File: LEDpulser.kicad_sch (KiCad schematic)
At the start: 70 parts, among them J1 RJHSE-5380, J2 EPS.00.250.NTN, J3 EPS.00.250.NTN, J4 EB21A-04-D, J5 EPL.0S.302.HLN, Q1 BVSS84LT1G, Q2 DMN3028LQ-7, Q3 DMN3028LQ-7, SW1 BST11T2AVR, U1 74AHCT123APW,118, U10 LT3082EST#TRPBF, U2 74AHCT123APW,118, U3 74AHCT123APW,118, U4 SN74LVC2G74, U5 LT1117, U6 IXDI602SIATR, U7 NE555S-13, U8 PM8834, U9 PM8834

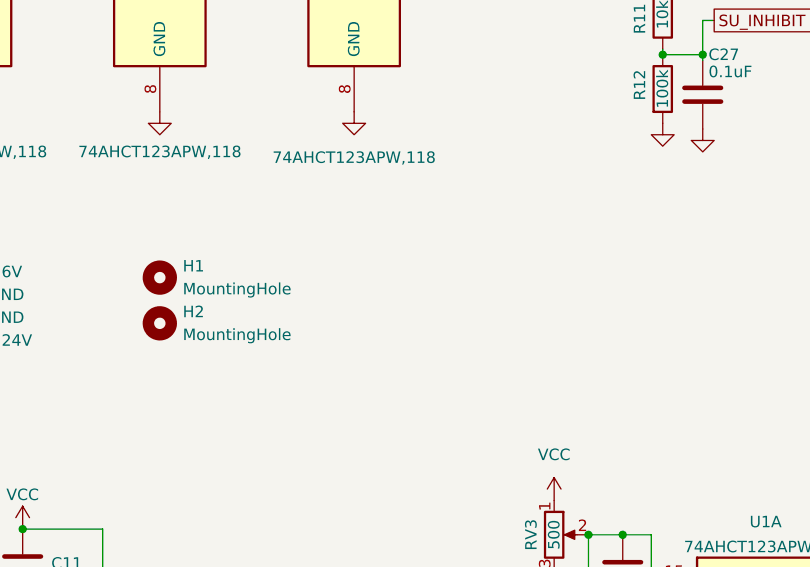
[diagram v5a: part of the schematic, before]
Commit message: Added third mounting hole. Added cutout for LEMO-connector back-side nuts.
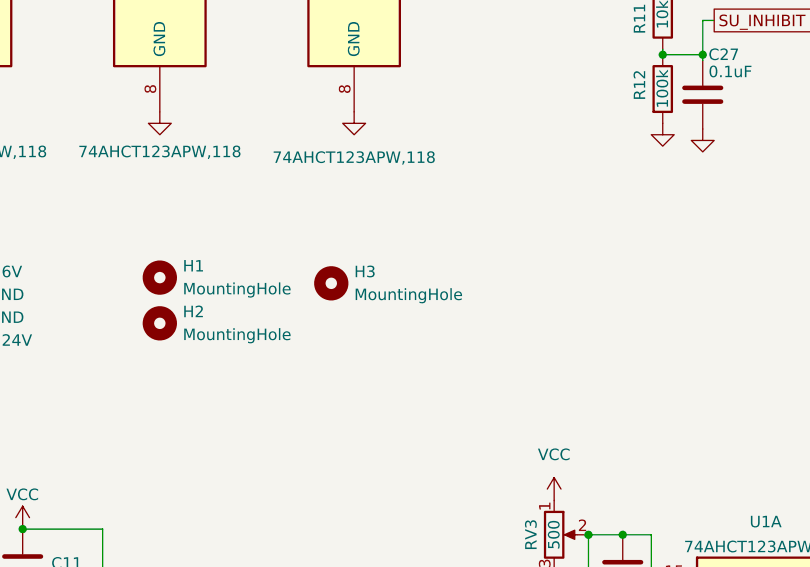
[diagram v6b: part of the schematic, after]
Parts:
- added H3: MountingHole, MountingHole:MountingHole_3.2mm_M3, symbol Mechanical:MountingHole
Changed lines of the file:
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@@
   (symbol (lib_id "power:VCC") (at 55.245 208.28 180) (unit 1)
     (in_bom yes) (on_board yes)
-    (property "Reference" "#PWR?" (id 0) (at 55.245 204.47 0)
+    (property "Reference" "#PWR0120" (id 0) (at 55.245 204.47 0)
       (effects (font (size 1.27 1.27)) hide)
     )
@@
     (pin "1")
   )
+  (symbol (lib_id "Mechanical:MountingHole") (at 72.39 64.77 0) (unit 1)
+    (in_bom yes) (on_board yes) (fields_autoplaced)
+    (property "Reference" "H3" (id 0) (at 74.93 63.4999 0)
+      (effects (font (size 1.27 1.27)) (justify left))
+    )
+    (property "Value" "MountingHole" (id 1) (at 74.93 66.0399 0)
+      (effects (font (size 1.27 1.27)) (justify left))
+    )
+    (property "Footprint" "MountingHole:MountingHole_3.2mm_M3" (id 2) (at 72.39 64.77 0)
+      (effects (font (size 1.27 1.27)) hide)
+    )
+    (property "Datasheet" "~" (id 3) (at 72.39 64.77 0)
+      (effects (font (size 1.27 1.27)) hide)
+    )
+  )
   (symbol (lib_id "power:VCC") (at 38.1 92.075 0) (unit 1)
     (in_bom yes) (on_board yes)
@@
       (reference "#PWR0119") (unit 1) (value "GND") (footprint "")
     )
+    (path "/3407777c-d948-490d-a2f0-b3ad3390e217"
+      (reference "#PWR0120") (unit 1) (value "VCC") (footprint "")
+    )
     (path "/b48ba73f-35c5-4fb7-bedf-312e98c2ff95"
       (reference "#PWR0121") (unit 1) (value "GND") (footprint "")
@@
       (reference "#PWR0177") (unit 1) (value "GND") (footprint "")
     )
-    (path "/3407777c-d948-490d-a2f0-b3ad3390e217"
-      (reference "#PWR?") (unit 1) (value "VCC") (footprint "")
-    )
     (path "/f93b1b9a-0026-469f-bb79-98b3a8c675dd"
       (reference "C1") (unit 1) (value "0.1uF") (footprint "Capacitor_SMD:C_0603_1608Metric")
@@
       (reference "H2") (unit 1) (value "MountingHole") (footprint "MountingHole:MountingHole_3.2mm_M3")
     )
+    (path "/7d646651-5aef-453f-ad93-710225b27da3"
+      (reference "H3") (unit 1) (value "MountingHole") (footprint "MountingHole:MountingHole_3.2mm_M3")
+    )
     (path "/9488ae24-3cd4-4e78-897c-a03dbef50cd8"

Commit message: Added series resistors for pots.
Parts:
- added R13: 22, Resistor_SMD:R_0603_1608Metric, symbol Device:R
- added R14, R15, R16, R17, R18, R19, R20, R21, R22, R23, R24: 0, Resistor_SMD:R_0603_1608Metric, symbol Device:R
- added R25: DNP, Resistor_SMD:R_0603_1608Metric, symbol Device:R
- Q1: value BVSS84LT1G -> DMP32D4S; VGS(th) VGS(th) -0.9V to -2.0V -> VGS(th) -1.4V to -2.4V
- R2: value 1k -> 10k
- RV1: value 2k -> 2Meg; Part# Y50532K00000J0L -> 3296Z-1-205LF; TemperatureCoefficient 10ppm/C -> 100ppm/C
- RV2, RV3: value 500 -> 2k
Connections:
- net CAP_CHARGING_OUT: now also R23.2; no longer Q1.1 (G)
- net CAP_VOLTAGE_OUT: now also R24.2; no longer Q1.2 (S)
- net LED_ON_OUT: now also R22.2; no longer Q2.1 (G)
- net LED_SHORT_OUT: now also R21.2; no longer Q3.1 (G)
- net VCC: now also R25.1
- net at C7.1, U10.1 (ADJ): now also R20.2; no longer RV1.2, RV1.3
- net at RV4.2, RV4.3: now also R18.1; no longer C14.1, U2.7 (RCext)
- net at RV3.2, RV3.3: now also R15.1; no longer C13.1, U1.15 (RCext)
- net at RV6.2, RV6.3: now also R17.1; no longer C19.1, U3.15 (RCext)
- net at C20.1, U3.7 (RCext): now also R19.2; no longer RV7.2, RV7.3
- net at C18.1, U7.2 (TR), U7.6 (THR): now also R13.2, R25.2; no longer RV5.2, RV5.3
- net at C8.2, U2.15 (RCext): now also R16.2; no longer RV2.2, RV2.3
- net at RV8.2, RV8.3: now also R14.2; no longer C25.1, U1.7 (RCext)
- new net: R13.1, RV5.2, RV5.3
- new net: Q1.2 (S), R24.1
- new net: C14.1, R18.2, U2.7 (RCext)
- new net: C13.1, R15.2, U1.15 (RCext)
- new net: R16.1, RV2.2, RV2.3
- new net: R19.1, RV7.2, RV7.3
- new net: C19.1, R17.2, U3.15 (RCext)
- new net: C25.1, R14.1, U1.7 (RCext)
- new net: Q1.1 (G), R23.1
- new net: Q2.1 (G), R22.1
- new net: Q3.1 (G), R21.1
- new net: R20.1, RV1.2, RV1.3
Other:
- moved on the sheet: C19, C24, C26, C5, C7, D2, J1, RV1, RV2, RV3, RV4, RV5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

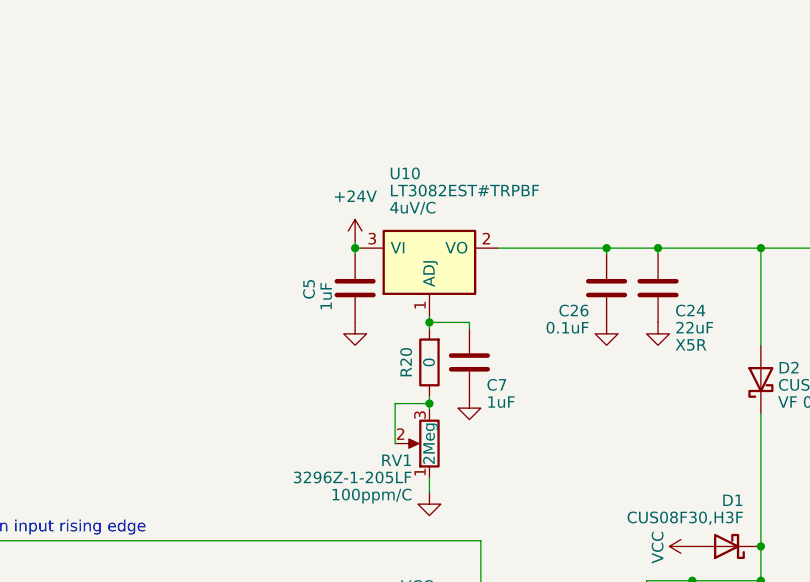
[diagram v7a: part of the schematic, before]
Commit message: Added guard ring around 0-20V regulator set pin and output to set current shunt.
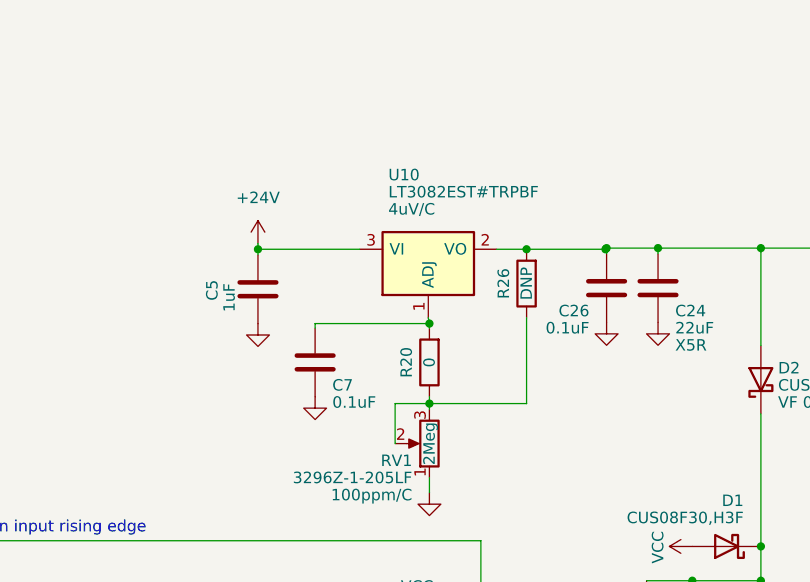
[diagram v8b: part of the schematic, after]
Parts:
- added R26: DNP, Resistor_SMD:R_0603_1608Metric, symbol Device:R
- C7: value 1uF -> 0.1uF; footprint Capacitor_SMD:C_0603_1608Metric -> Capacitor_SMD:C_0805_2012Metric
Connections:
- net CAP_VOLTAGE_OUT: now also R26.2
- net at R20.1, RV1.2, RV1.3: now also R26.1
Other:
- moved on the sheet: C5, C7
